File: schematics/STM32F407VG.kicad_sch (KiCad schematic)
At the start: 19 parts, among them SW1 SW_DPST_x2, X2 8MHz

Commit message: Множественные обновления схем
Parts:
- added LD202: ~, LED_SMD:LED_0805_2012Metric, symbol Device:LED
- added Q1, Q41: MMBT3904, PCM_4ms_Package_SOT:SOT-23, symbol PCM_Transistor_BJT_AKL:MMBT3904
- added R10, R11, R3, R4, R5, R6, R7, R8, R9: 10, Resistor_SMD:R_1206_3216Metric_Pad1.30x1.75mm_HandSolder, symbol Device:R
- added R205: 1k, Resistor_SMD:R_0805_2012Metric, symbol Device:R
- added R747, R748, R749: 10k, Resistor_SMD:R_0805_2012Metric, symbol Device:R
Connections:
- net +3.3V: now also R205.2
- net GND: now also Q1.2 (E), Q41.2 (E)
- net PA10: now also R11.1; no longer MK2.69 (PA10)
- net PA8: now also LD202.1 (K)
- net PA9: now also R10.1; no longer MK2.68 (PA9)
- net PB11: now also R3.1; no longer MK2.48 (PB11)
- net PB12: now also R4.1; no longer MK2.51 (PB12)
- net PB13: now also R5.1; no longer MK2.52 (PB13)
- net PB14: now also R6.1; no longer MK2.53 (PB14)
- net PB15: now also R7.1; no longer MK2.54 (PB15)
- net PD4: now also R747.2
- net PD5: now also R8.2; no longer MK2.86 (PD5)
- net PD6: now also R9.2; no longer MK2.87 (PD6)
- new net: LD202.2 (A), R205.1
- new net: MK2.48 (PB11), R3.2
- new net: Q1.3 (C), Q41.1 (B), R748.1
- new net: Q1.1 (B), R747.1
- new net: MK2.54 (PB15), R7.2
- new net: MK2.51 (PB12), R4.2
- new net: MK2.52 (PB13), R5.2
- new net: MK2.87 (PD6), R9.1
- new net: MK2.69 (PA10), R11.2
- new net: MK2.86 (PD5), R8.1
- new net: MK2.53 (PB14), R6.2
- new net: MK2.68 (PA9), R10.2
- new net +5V: R748.2, R749.2
- new net EN: Q41.3 (C), R749.1
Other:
- company: Филимонов и К -> (none)
- title: (none) -> OctopusNode

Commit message: Обновил обозначения, а то старая нумерация была специфической
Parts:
- C16: renamed from C10; footprint Capacitor_SMD:C_1206_3216Metric_Pad1.33x1.80mm_HandSolder -> Capacitor_SMD:C_0805_2012Metric
- C17: renamed from C11; footprint Capacitor_SMD:C_1206_3216Metric_Pad1.33x1.80mm_HandSolder -> Capacitor_SMD:C_0805_2012Metric
- C18: renamed from C3; footprint Capacitor_SMD:C_1206_3216Metric_Pad1.33x1.80mm_HandSolder -> Capacitor_SMD:C_0805_2012Metric
- C19: renamed from C4; footprint Capacitor_SMD:C_1206_3216Metric_Pad1.33x1.80mm_HandSolder -> Capacitor_SMD:C_0805_2012Metric
- C20: renamed from C5; footprint Capacitor_SMD:C_1206_3216Metric_Pad1.33x1.80mm_HandSolder -> Capacitor_SMD:C_0805_2012Metric
- C21: renamed from C1; footprint Capacitor_SMD:C_1206_3216Metric_Pad1.33x1.80mm_HandSolder -> Capacitor_SMD:C_0805_2012Metric
- C22: renamed from C2; footprint Capacitor_SMD:C_1206_3216Metric_Pad1.33x1.80mm_HandSolder -> Capacitor_SMD:C_0805_2012Metric
- C23: renamed from C6; footprint Capacitor_SMD:C_1206_3216Metric_Pad1.33x1.80mm_HandSolder -> Capacitor_SMD:C_0805_2012Metric
- C24: renamed from C31; footprint Capacitor_SMD:C_1206_3216Metric_Pad1.33x1.80mm_HandSolder -> Capacitor_SMD:C_0805_2012Metric
- C25: renamed from C32; footprint Capacitor_SMD:C_1206_3216Metric_Pad1.33x1.80mm_HandSolder -> Capacitor_SMD:C_0805_2012Metric
- C26: renamed from C7; footprint Capacitor_SMD:C_1206_3216Metric_Pad1.33x1.80mm_HandSolder -> Capacitor_SMD:C_0805_2012Metric
- C27: renamed from C8; footprint Capacitor_SMD:C_1206_3216Metric_Pad1.33x1.80mm_HandSolder -> Capacitor_SMD:C_0805_2012Metric
- C28: renamed from C9; footprint Capacitor_SMD:C_1206_3216Metric_Pad1.33x1.80mm_HandSolder -> Capacitor_SMD:C_0805_2012Metric
- R16: renamed from R1; footprint Resistor_SMD:R_1206_3216Metric_Pad1.30x1.75mm_HandSolder -> Resistor_SMD:R_0805_2012Metric
- renumbered C33 to C15, LD202 to LD5, Q41 to Q2, R746 to R13, R8 to R14, R9 to R15, R10 to R17, R11 to R18, R3 to R19, R4 to R20, R5 to R21, R6 to R22, R7 to R23, R205 to R24, R747 to R25, R748 to R26, R749 to R27, MK2 to U5, X2 to X1

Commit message: Было еще что-то 1206
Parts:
- R14, R15, R17, R18, R19, R20, R21, R22, R23: footprint Resistor_SMD:R_1206_3216Metric_Pad1.30x1.75mm_HandSolder -> Resistor_SMD:R_0805_2012Metric
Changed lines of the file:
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@@
 			)
 		)
-		(property "Footprint" "Resistor_SMD:R_1206_3216Metric_Pad1.30x1.75mm_HandSolder"
+		(property "Footprint" "Resistor_SMD:R_0805_2012Metric"
 			(at 143.51 101.092 90)
 			(effects
@@
 			)
 		)
-		(property "Footprint" "Resistor_SMD:R_1206_3216Metric_Pad1.30x1.75mm_HandSolder"
+		(property "Footprint" "Resistor_SMD:R_0805_2012Metric"
 			(at 143.51 111.252 90)
 			(effects
@@
 			)
 		)
-		(property "Footprint" "Resistor_SMD:R_1206_3216Metric_Pad1.30x1.75mm_HandSolder"
+		(property "Footprint" "Resistor_SMD:R_0805_2012Metric"
 			(at 143.51 103.632 90)
 			(effects
@@
 			)
 		)
-		(property "Footprint" "Resistor_SMD:R_1206_3216Metric_Pad1.30x1.75mm_HandSolder"
+		(property "Footprint" "Resistor_SMD:R_0805_2012Metric"
 			(at 143.51 106.172 90)
 			(effects
@@
 			)
 		)
-		(property "Footprint" "Resistor_SMD:R_1206_3216Metric_Pad1.30x1.75mm_HandSolder"
+		(property "Footprint" "Resistor_SMD:R_0805_2012Metric"
 			(at 55.88 111.252 90)
 			(effects
@@
 			)
 		)
-		(property "Footprint" "Resistor_SMD:R_1206_3216Metric_Pad1.30x1.75mm_HandSolder"
+		(property "Footprint" "Resistor_SMD:R_0805_2012Metric"
 			(at 143.51 55.372 90)
 			(effects
@@
 			)
 		)
-		(property "Footprint" "Resistor_SMD:R_1206_3216Metric_Pad1.30x1.75mm_HandSolder"
+		(property "Footprint" "Resistor_SMD:R_0805_2012Metric"
 			(at 55.88 108.712 90)
 			(effects
@@
 			)
 		)
-		(property "Footprint" "Resistor_SMD:R_1206_3216Metric_Pad1.30x1.75mm_HandSolder"
+		(property "Footprint" "Resistor_SMD:R_0805_2012Metric"
 			(at 143.51 108.712 90)
 			(effects
@@
 			)
 		)
-		(property "Footprint" "Resistor_SMD:R_1206_3216Metric_Pad1.30x1.75mm_HandSolder"
+		(property "Footprint" "Resistor_SMD:R_0805_2012Metric"
 			(at 143.51 52.832 90)
 			(effects

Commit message: Правки схем, возможно что-то было не корректно выбрано
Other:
- moved on the sheet: C18, C19, C20, C21, C22, C23, C24, C25, C26, C27, C28, Q1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

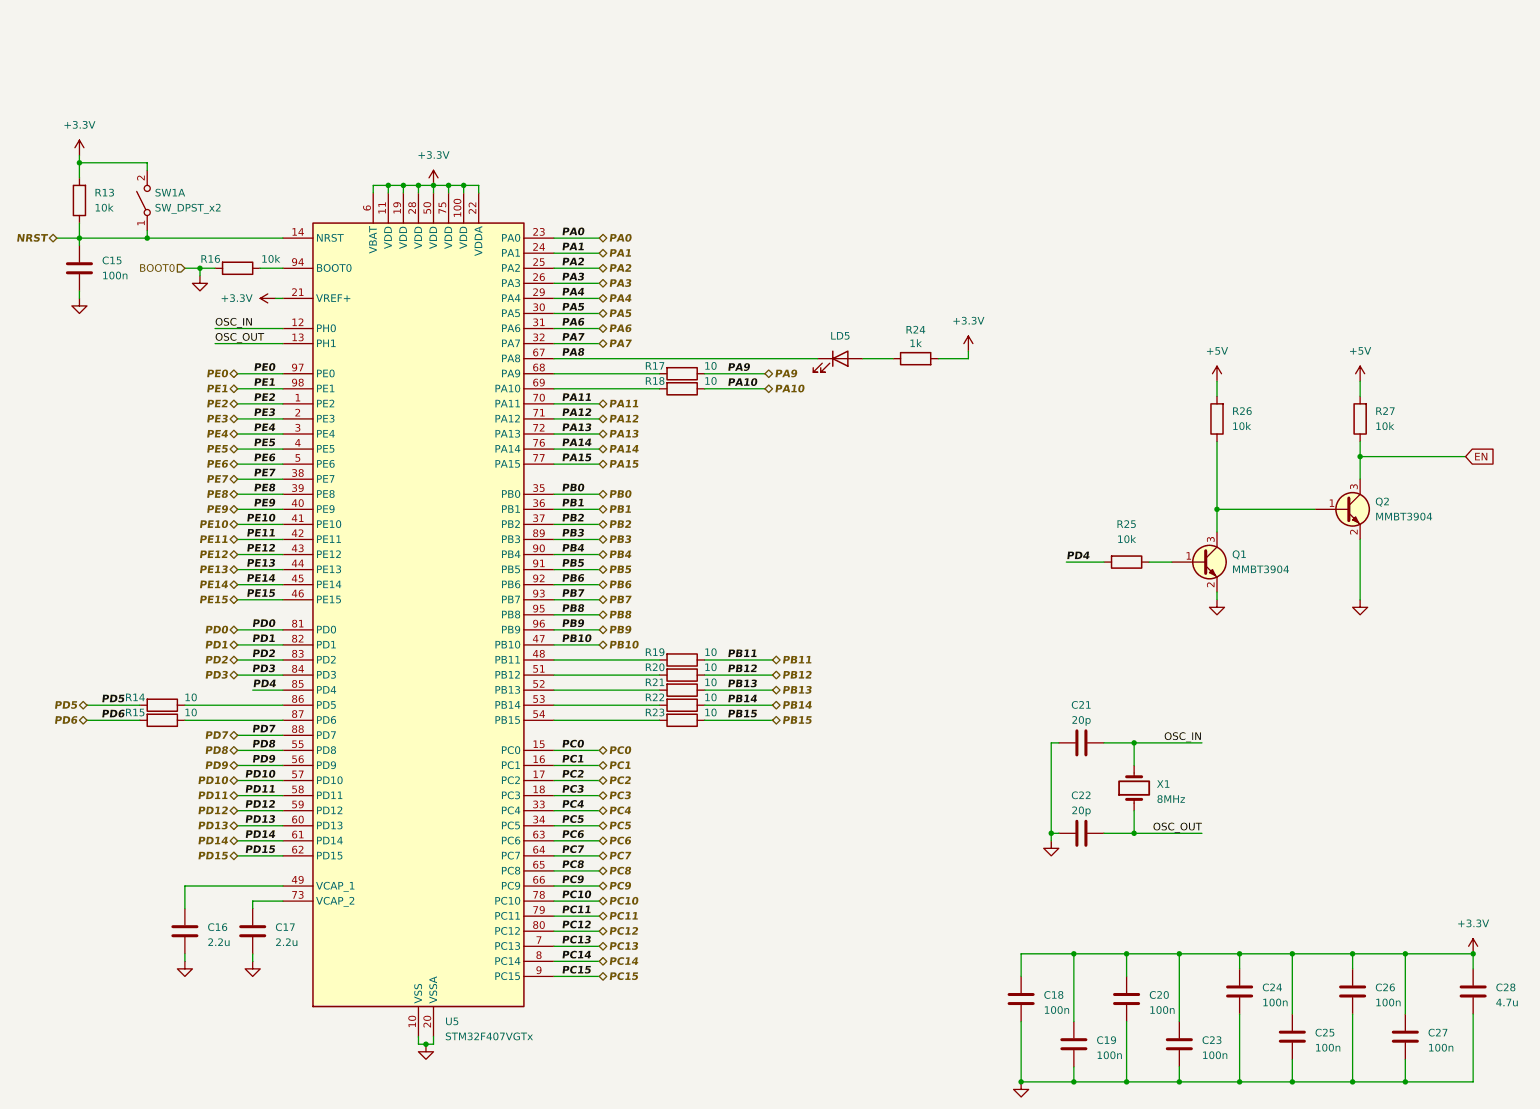
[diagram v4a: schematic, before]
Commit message: Переподключения, для оптимальной трассировки
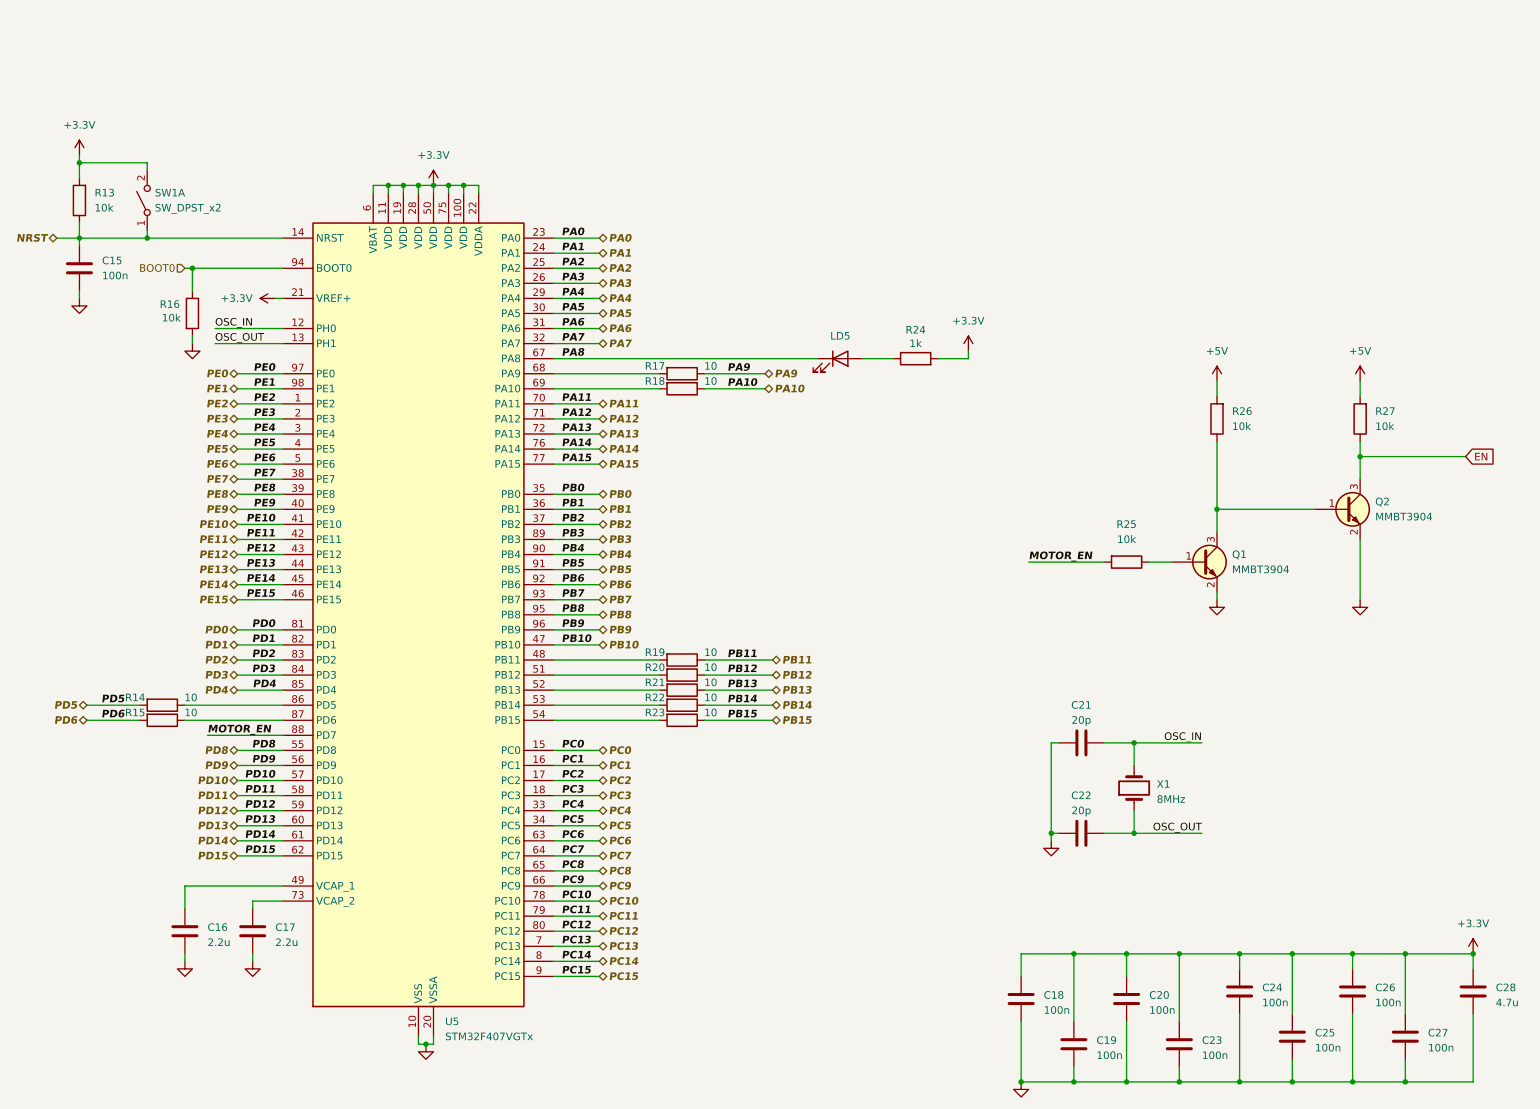
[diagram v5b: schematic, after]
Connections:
- net PD4: no longer R25.2
- net BOOT0: now reaches R16.1, U5.94 (BOOT0)
- net PD7 renamed MOTOR_EN
- net MOTOR_EN: now also R25.2
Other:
- moved on the sheet: R16
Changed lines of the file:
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@@
 	)
 	(junction
-		(at 218.44 152.4)
+		(at 60.96 36.83)
 		(diameter 0)
 		(color 0 0 0 0)
 	)
 	(junction
-		(at 62.23 36.83)
+		(at 218.44 152.4)
 		(diameter 0)
 		(color 0 0 0 0)
@@
 	(wire
 		(pts
-			(xy 68.58 115.57) (xy 76.2 115.57)
+			(xy 63.5 115.57) (xy 76.2 115.57)
 		)
 		(stroke
@@
 	(wire
 		(pts
+			(xy 59.69 36.83) (xy 60.96 36.83)
+		)
+		(stroke
+			(width 0)
+			(type default)
+		)
+	)
+	(wire
+		(pts
 			(xy 218.44 152.4) (xy 218.44 156.21)
 		)
@@
 	(wire
 		(pts
-			(xy 209.55 152.4) (xy 209.55 163.83)
+			(xy 68.58 107.95) (xy 76.2 107.95)
 		)
 		(stroke
@@
 	(wire
 		(pts
-			(xy 250.19 77.47) (xy 233.68 77.47)
+			(xy 209.55 152.4) (xy 209.55 163.83)
 		)
 		(stroke
@@
 	(wire
 		(pts
-			(xy 218.44 173.99) (xy 227.33 173.99)
+			(xy 250.19 77.47) (xy 233.68 77.47)
 		)
 		(stroke
@@
 	(wire
 		(pts
-			(xy 121.92 125.73) (xy 129.54 125.73)
+			(xy 218.44 173.99) (xy 227.33 173.99)
 		)
 		(stroke
@@
 	(wire
 		(pts
-			(xy 68.58 100.33) (xy 76.2 100.33)
+			(xy 121.92 125.73) (xy 129.54 125.73)
 		)
 		(stroke
@@
 	(wire
 		(pts
-			(xy 53.34 20.32) (xy 53.34 19.05)
+			(xy 68.58 100.33) (xy 76.2 100.33)
 		)
 		(stroke
@@
 	(wire
 		(pts
-			(xy 59.69 36.83) (xy 62.23 36.83)
+			(xy 53.34 20.32) (xy 53.34 19.05)
 		)
 		(stroke
@@
 	(wire
 		(pts
+			(xy 60.96 36.83) (xy 60.96 40.64)
+		)
+		(stroke
+			(width 0)
+			(type default)
+		)
+	)
+	(wire
+		(pts
 			(xy 68.58 59.69) (xy 76.2 59.69)
 		)
@@
 	(wire
 		(pts
-			(xy 71.12 107.95) (xy 76.2 107.95)
-		)
-		(stroke
-			(width 0)
-			(type default)
-		)
-	)
-	(wire
-		(pts
-			(xy 72.39 36.83) (xy 76.2 36.83)
-		)
-		(stroke
-			(width 0)
-			(type default)
-		)
-	)
-	(wire
-		(pts
 			(xy 121.92 69.85) (xy 129.54 69.85)
 		)
@@
 	(wire
 		(pts
+			(xy 60.96 36.83) (xy 76.2 36.83)
+		)
+		(stroke
+			(width 0)
+			(type default)
+		)
+	)
+	(wire
+		(pts
 			(xy 219.71 128.27) (xy 219.71 132.08)
 		)
@@
 	(wire
 		(pts
-			(xy 62.23 36.83) (xy 62.23 38.1)
+			(xy 60.96 48.26) (xy 60.96 49.53)
 		)
 		(stroke
@@
 	(wire
 		(pts
-			(xy 208.28 86.36) (xy 214.63 86.36)
+			(xy 201.93 86.36) (xy 214.63 86.36)
 		)
 		(stroke
@@
 	(wire
 		(pts
-			(xy 62.23 36.83) (xy 64.77 36.83)
-		)
-		(stroke
-			(width 0)
-			(type default)
-		)
-	)
-	(wire
-		(pts
 			(xy 121.92 143.51) (xy 129.54 143.51)
 		)
@@
 		)
 	)
-	(label "PD4"
-		(at 208.28 86.36 0)
-		(effects
-			(font
-				(size 1.27 1.27)
-				(bold yes)
-				(italic yes)
-			)
-			(justify left bottom)
-		)
-	)
 	(label "PD9"
 		(at 74.93 120.65 180)
@@
 		)
 	)
-	(label "PD7"
-		(at 74.93 115.57 180)
-		(effects
-			(font
-				(size 1.27 1.27)
-				(bold yes)
-				(italic yes)
-			)
-			(justify right bottom)
-		)
-	)
 	(label "OSC_OUT"
 		(at 231.14 132.08 180)
@@
 		)
 	)
+	(label "MOTOR_EN"
+		(at 63.5 115.57 0)
+		(effects
+			(font
+				(size 1.27 1.27)
+				(bold yes)
+				(italic yes)
+			)
+			(justify left bottom)
+		)
+	)
 	(label "PC13"
 		(at 123.19 151.13 0)
@@
 		)
 	)
+	(label "MOTOR_EN"
+		(at 201.93 86.36 0)
+		(effects
+			(font
+				(size 1.27 1.27)
+				(bold yes)
+				(italic yes)
+			)
+			(justify left bottom)
+		)
+	)
 	(label "PE6"
 		(at 74.93 69.85 180)
@@
 		)
 	)
+	(hierarchical_label "PD4"
+		(shape bidirectional)
+		(at 68.58 107.95 180)
+		(effects
+			(font
+				(size 1.27 1.27)
+				(bold yes)
+				(italic yes)
+			)
+			(justify right)
+		)
+	)
 	(hierarchical_label "PA0"
 		(shape bidirectional)
@@
 		)
 	)
-	(hierarchical_label "PD7"
-		(shape bidirectional)
-		(at 68.58 115.57 180)
-		(effects
-			(font
-				(size 1.27 1.27)
-				(bold yes)
-				(italic yes)
-			)
-			(justify right)
-		)
-	)
 	(hierarchical_label "PE5"
 		(shape bidirectional)
@@
 	(symbol
 		(lib_id "Device:R")
-		(at 68.58 36.83 270)
+		(at 60.96 44.45 0)
 		(unit 1)
 		(exclude_from_sim no)
@@
 		(dnp no)
 		(property "Reference" "R16"
-			(at 64.008 35.306 90)
+			(at 57.15 42.926 0)
 			(effects
 				(font
@@
 		)
 		(property "Value" "10k"
-			(at 74.168 35.306 90)
+			(at 57.404 45.212 0)
 			(effects
 				(font
@@
 		)
 		(property "Footprint" "Resistor_SMD:R_0805_2012Metric"
-			(at 68.58 35.052 90)
+			(at 59.182 44.45 90)
 			(effects
 				(font
@@
 		)
 		(property "Datasheet" "~"
-			(at 68.58 36.83 0)
+			(at 60.96 44.45 0)
 			(effects
 				(font
@@
 		)
 		(property "Description" ""
-			(at 68.58 36.83 0)
+			(at 60.96 44.45 0)
 			(effects
 				(font
@@
 	(symbol
 		(lib_id "power:GND")
-		(at 62.23 38.1 0)
+		(at 60.96 49.53 0)
 		(unit 1)
 		(exclude_from_sim no)
@@
 		(fields_autoplaced yes)
 		(property "Reference" "#PWR062"
-			(at 62.23 44.45 0)
+			(at 60.96 55.88 0)
 			(effects
 				(font
@@
 		)
 		(property "Value" "GND"
-			(at 62.23 43.18 0)
+			(at 60.96 54.61 0)
 			(effects
 				(font
@@
 		)
 		(property "Footprint" ""
-			(at 62.23 38.1 0)
+			(at 60.96 49.53 0)
 			(effects
 				(font
@@
 		)
 		(property "Datasheet" ""
-			(at 62.23 38.1 0)
+			(at 60.96 49.53 0)
 			(effects
 				(font
@@
 		)
 		(property "Description" "Power symbol creates a global label with name \"GND\" , ground"
-			(at 62.23 38.1 0)
+			(at 60.96 49.53 0)
 			(effects
 				(font
